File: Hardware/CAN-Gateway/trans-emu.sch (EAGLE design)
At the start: 33 parts, among them IC1 MIC5233-3.3YM5-TR, U1 STM32F413RGT6, U2 TJA1042HVSON, U3 TJA1042HVSON, U4 TJA1042HVSON, Y1 CRYSTAL-3.2X2.54-PIN

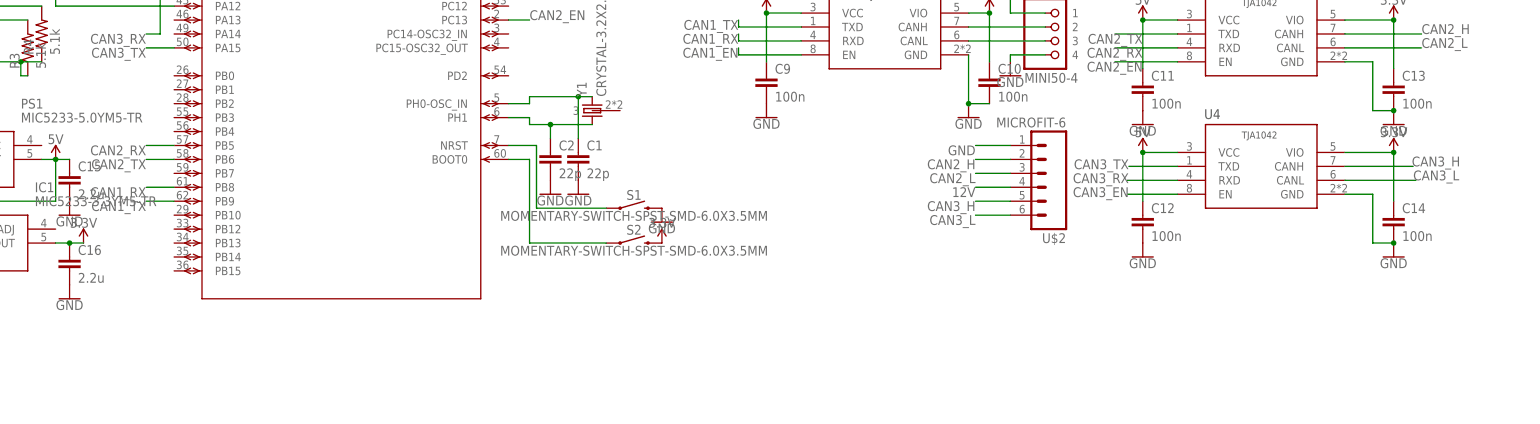
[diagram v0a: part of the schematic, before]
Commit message: Ibooster board updates
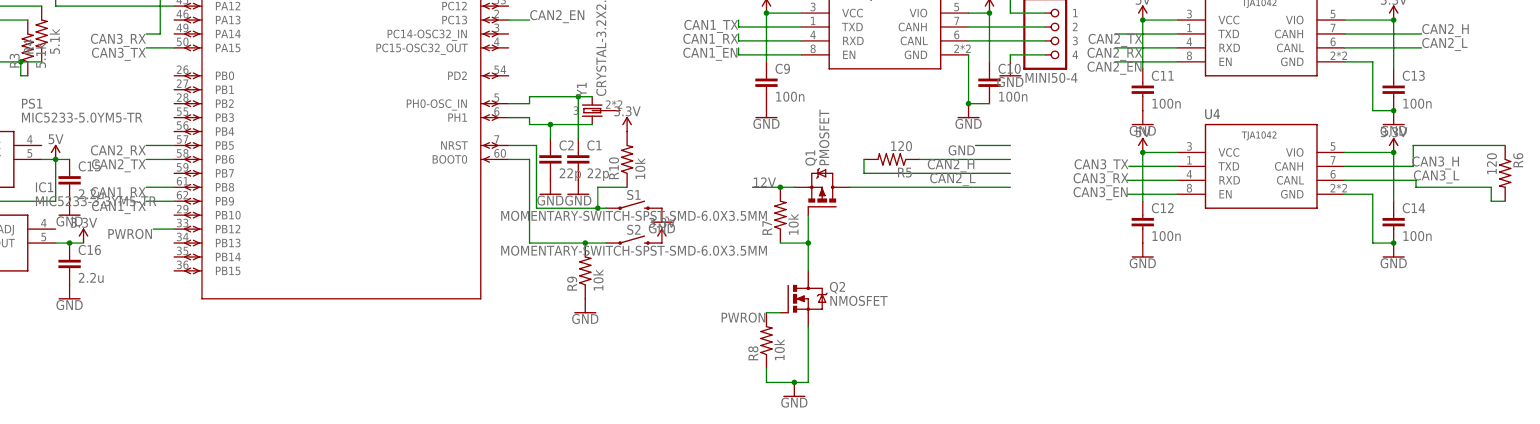
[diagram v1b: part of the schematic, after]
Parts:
- removed U$2: MICROFIT-6, interceptor:MICROFIT-6
- added Q1: PMOSFET, Transistor:PMOSFET_SOT23
- added Q2: NMOSFET, Transistor:NMOSFETSOT23
- added R10, R7, R8, R9: 10k, comma.ai:R0402
- added R5, R6: 120, comma.ai:R0402
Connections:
- new net N$15: Q1.D
- new net N$16: Q1.G, Q2.D, R7.1
- new net PWRON: Q2.G, R8.2, U1A.PB12
- net 12V: now also Q1.S, R7.2; no longer U$2.4
- net 3.3V: now also R10.2
- net CAN2_H: now also R5.1; no longer U$2.2
- net CAN2_L: now also R5.2; no longer U$2.3
- net CAN3_H: now also R6.1; no longer U$2.5
- net CAN3_L: now also R6.2; no longer U$2.6
- net GND: now also Q2.S, R8.1, R9.1; no longer U$2.1
- net N$8: now also R10.1
- net N$9: now also R9.2

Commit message: Gateway rev2
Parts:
- removed U$1: MINI50-4, interceptor:MINI50-4
- added J2, J3, J4: (no value), SparkFun-Connectors:CONN_02
- added J5: (no value), SparkFun-Connectors:CONN_04
- added SJ1, SJ2: (no value), jumper:SJ
- U2, U3, U4: value TJA1042HVSON -> TJA1042; device comma.ai:TJA1042HVSON -> CM,118:TJA1042
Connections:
- removed net N$15: Q1.D
- new net 12VOUT: J3.1, Q1.D
- new net CAN1_H: J4.1, U2.CANH
- new net CAN1_L: J4.2, U2.CANL
- net 12V: now also J2.1; no longer U$1.1
- net CAN2_H: now also J5.1
- net CAN2_L: now also J5.2, SJ1.1; no longer R5.2
- net CAN3_H: now also J5.3, SJ2.1; no longer R6.1
- net CAN3_L: now also J5.4
- net GND: now also J2.2, J3.2; no longer U$1.4
- net N$12: now also R5.2, SJ1.2; no longer U$1.2, U2.CANH
- net N$14: now also R6.1, SJ2.2; no longer U$1.3, U2.CANL
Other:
- moved on the sheet: R5, U2, U3, U4

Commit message: swd header
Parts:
- added J6: (no value), SparkFun-Connectors:CONN_051.27MM
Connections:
- removed net N$8: R10.1, S1.1, U1A.NRST
- new net NRST: J6.4, R10.1, S1.1, U1A.NRST
- new net SCK: J6.2, U1A.PA14
- new net SWD: J6.3, U1A.PA13
- net 3.3V: now also J6.5
- net GND: now also J6.1
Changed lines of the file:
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@@
 <part name="GND5" library="SparkFun-PowerSymbols" library_urn="urn:adsk.eagle:library:530" deviceset="GND" device=""/>
 <part name="GND20" library="SparkFun-PowerSymbols" library_urn="urn:adsk.eagle:library:530" deviceset="GND" device=""/>
+<part name="J6" library="SparkFun-Connectors" library_urn="urn:adsk.eagle:library:513" deviceset="CONN_05" device="1.27MM" package3d_urn="urn:adsk.eagle:package:38110/1"/>
+<part name="SUPPLY15" library="SparkFun-PowerSymbols" library_urn="urn:adsk.eagle:library:530" deviceset="3.3V" device=""/>
+<part name="GND21" library="SparkFun-PowerSymbols" library_urn="urn:adsk.eagle:library:530" deviceset="GND" device=""/>
 </parts>
 <sheets>
@@
 <instance part="GND20" gate="1" x="177.8" y="-20.32" smashed="yes">
 <attribute name="VALUE" x="177.8" y="-20.574" size="1.778" layer="96" align="top-center"/>
+</instance>
+<instance part="J6" gate="G$1" x="12.7" y="-22.86" smashed="yes">
+<attribute name="VALUE" x="10.16" y="-32.766" size="1.778" layer="96" font="vector"/>
+<attribute name="NAME" x="10.16" y="-14.732" size="1.778" layer="95" font="vector"/>
+</instance>
+<instance part="SUPPLY15" gate="G$1" x="25.4" y="-17.78" smashed="yes">
+<attribute name="VALUE" x="25.4" y="-14.986" size="1.778" layer="96" align="bottom-center"/>
+</instance>
+<instance part="GND21" gate="1" x="22.86" y="-30.48" smashed="yes">
+<attribute name="VALUE" x="22.86" y="-30.734" size="1.778" layer="96" align="top-center"/>
 </instance>
 </instances>
@@
 <pinref part="GND20" gate="1" pin="GND"/>
 </segment>
+<segment>
+<pinref part="J6" gate="G$1" pin="1"/>
+<wire x1="22.86" y1="-27.94" x2="20.32" y2="-27.94" width="0.1524" layer="91"/>
+<pinref part="GND21" gate="1" pin="GND"/>
+</segment>
 </net>
 <net name="CAN1_RX" class="0">
@@
 <segment>
 <pinref part="U1" gate="A" pin="PA8"/>
-<wire x1="31.75" y1="63.5" x2="29.21" y2="63.5" width="0.1524" layer="91"/>
-<wire x1="29.21" y1="63.5" x2="29.21" y2="48.26" width="0.1524" layer="91"/>
-<wire x1="29.21" y1="48.26" x2="26.67" y2="48.26" width="0.1524" layer="91"/>
-<label x="26.67" y="48.26" size="1.778" layer="95" rot="R180"/>
+<wire x1="31.75" y1="63.5" x2="26.67" y2="63.5" width="0.1524" layer="91"/>
+<label x="26.67" y="63.5" size="1.778" layer="95" rot="R180"/>
 </segment>
 <segment>
@@
 </segment>
 </net>
-<net name="N$8" class="0">
+<net name="NRST" class="0">
 <segment>
 <pinref part="U1" gate="A" pin="NRST"/>
@@
 <wire x1="108.966" y1="20.32" x2="108.966" y2="16.51" width="0.1524" layer="91"/>
 <junction x="108.966" y="16.51"/>
+<label x="96.52" y="27.94" size="1.778" layer="95"/>
+</segment>
+<segment>
+<pinref part="J6" gate="G$1" pin="4"/>
+<wire x1="20.32" y1="-20.32" x2="25.4" y2="-20.32" width="0.1524" layer="91"/>
+<label x="25.4" y="-20.32" size="1.778" layer="95"/>
 </segment>
 </net>
@@
 <pinref part="SUPPLY14" gate="G$1" pin="3.3V"/>
 </segment>
+<segment>
+<pinref part="J6" gate="G$1" pin="5"/>
+<pinref part="SUPPLY15" gate="G$1" pin="3.3V"/>
+<wire x1="20.32" y1="-17.78" x2="25.4" y2="-17.78" width="0.1524" layer="91"/>
+</segment>
 </net>
 <net name="12V" class="0">
@@
 </segment>
 </net>
+<net name="SWD" class="0">
+<segment>
+<pinref part="U1" gate="A" pin="PA13"/>
+<wire x1="31.75" y1="50.8" x2="27.94" y2="50.8" width="0.1524" layer="91"/>
+<label x="25.4" y="50.8" size="1.778" layer="95" rot="R180"/>
+</segment>
+<segment>
+<pinref part="J6" gate="G$1" pin="3"/>
+<wire x1="20.32" y1="-22.86" x2="25.4" y2="-22.86" width="0.1524" layer="91"/>
+<label x="25.4" y="-22.86" size="1.778" layer="95"/>
+</segment>
+</net>
+<net name="SCK" class="0">
+<segment>
+<pinref part="U1" gate="A" pin="PA14"/>
+<wire x1="31.75" y1="48.26" x2="27.94" y2="48.26" width="0.1524" layer="91"/>
+<label x="25.4" y="48.26" size="1.778" layer="95" rot="R180"/>
+</segment>
+<segment>
+<pinref part="J6" gate="G$1" pin="2"/>
+<wire x1="20.32" y1="-25.4" x2="25.4" y2="-25.4" width="0.1524" layer="91"/>
+<label x="25.4" y="-25.4" size="1.778" layer="95"/>
+</segment>
+</net>
